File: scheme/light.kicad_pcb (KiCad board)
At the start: 2 copper layers, 25 parts, among them J1 Screw_Terminal_01x04 (buttons), J2 Conn_01x06_Male (programmer), J3 Screw_Terminal_01x06 (output), J4 Conn_01x02_Male (i2c), J5 Conn_01x02_Male (Jumper), J6 Conn_01x03_Male (Indicators), J7 Screw_Terminal_01x02 (power), Q1 IRF8308M, Q2 IRF8308M, Q3 IRF8308M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

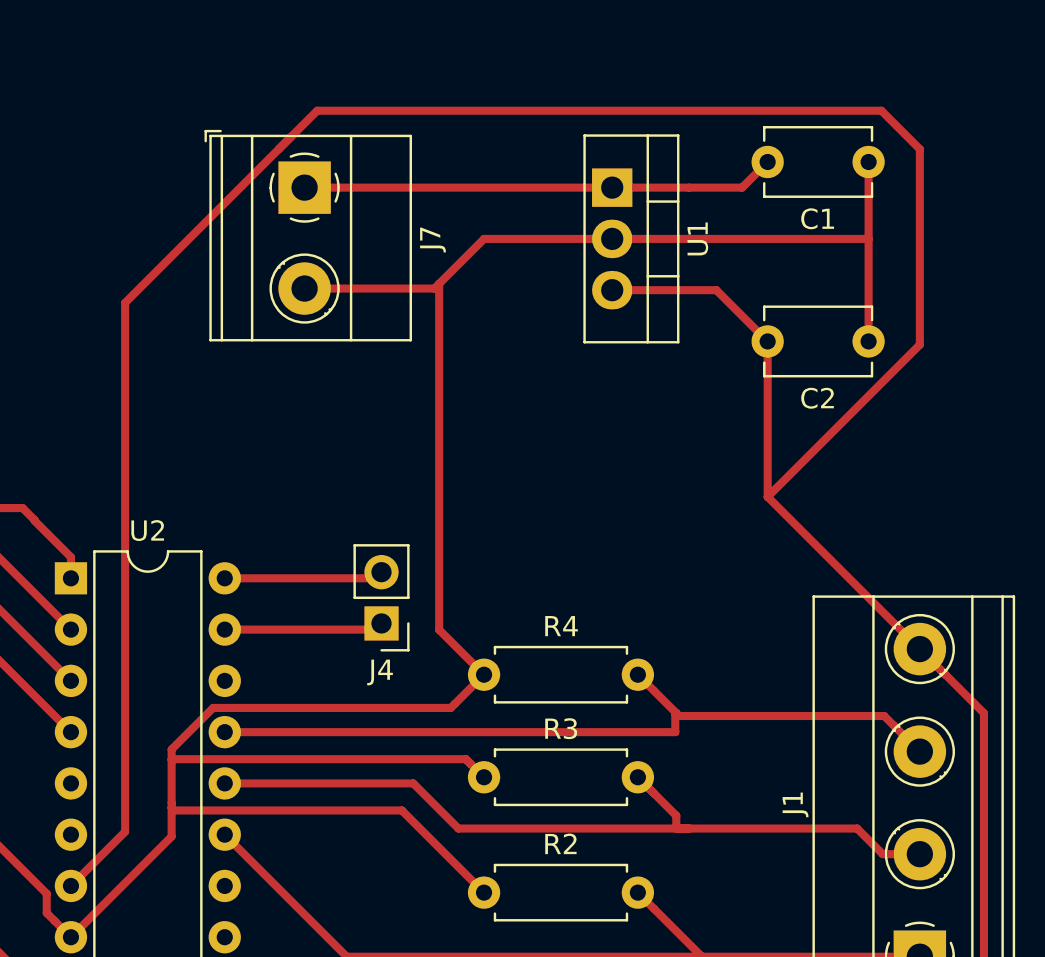
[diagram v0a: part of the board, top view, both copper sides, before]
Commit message: labels: fix power screw terminal orientation
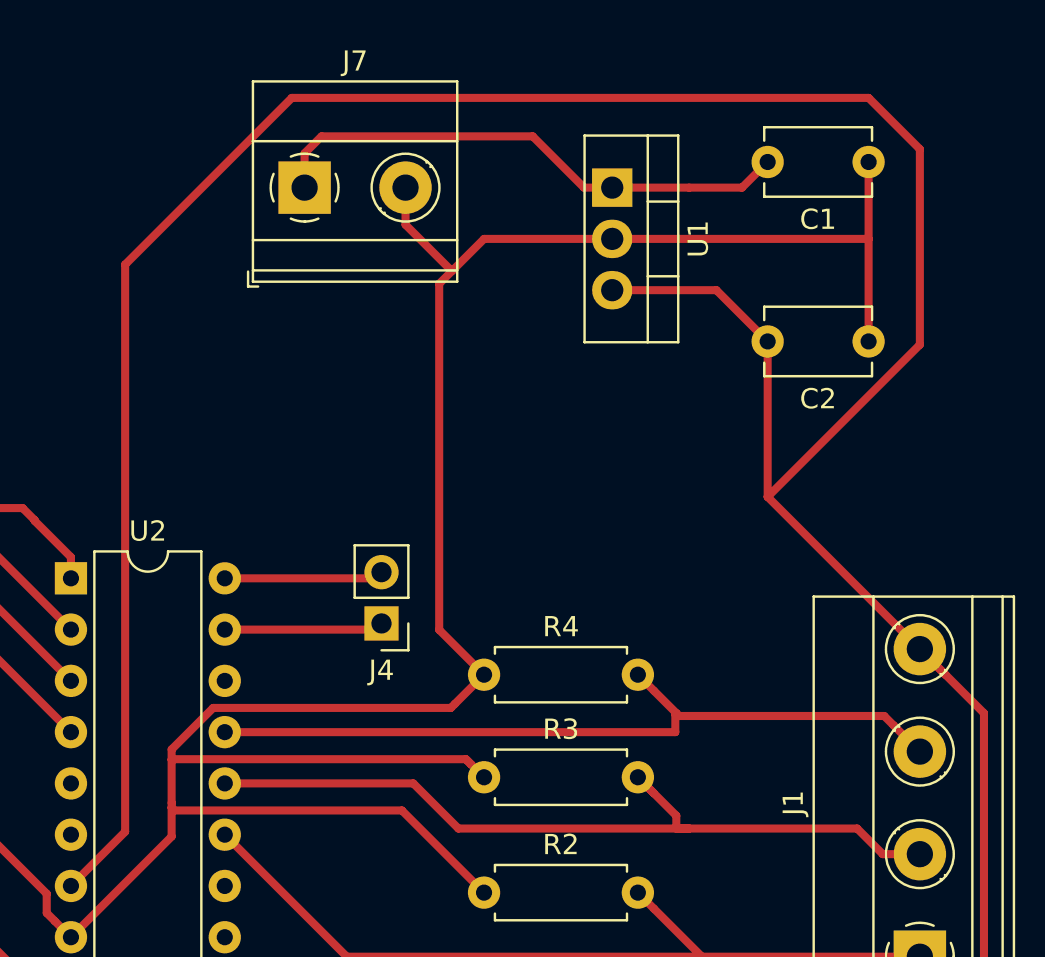
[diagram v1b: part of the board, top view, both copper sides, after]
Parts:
- turned J7 to 0 degrees
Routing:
- net Net-(C1-Pad2): track 23.5 -> 26.6 mm
- net GND: track 259.6 -> 257.9 mm
- net Net-(C2-Pad2): track 238.3 -> 239.1 mm
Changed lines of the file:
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@@
   (general
     (thickness 1.6)
-    (drawings 0)
-    (tracks 208)
+    (drawings 2)
+    (tracks 211)
     (zones 0)
     (modules 25)
@@
   )
   (module TerminalBlock_Phoenix:TerminalBlock_Phoenix_MKDS-1,5-2_1x02_P5.00mm_Horizontal (layer F.Cu)
-    (at 148.59 43.18 270)
+    (at 148.59 43.18)
     (descr "Terminal Block Phoenix MKDS-1,5-2, 2 pins, pitch 5mm, size 10x9.8mm^2, drill diamater 1.3mm, pad diameter 2.6mm, see http://www.farnell.com/datasheets/100425.pdf, script-generated using https://github.com/pointhi/kicad-footprint-generator/scripts/TerminalBlock_Phoenix")
     (tags "THT Terminal Block Phoenix MKDS-1,5-2 pitch 5mm size 10x9.8mm^2 drill 1.3mm pad 2.6mm")
-    (fp_text reference J7 (at 2.5 -6.26 90) (layer F.SilkS)
-      (effects (font (size 1 1) (thickness 0.15)))
-    )
-    (fp_text value "Screw_Terminal_01x02 (power)" (at 2.5 5.66 90) (layer F.Fab)
+    (fp_text reference J7 (at 2.5 -6.26) (layer F.SilkS)
+      (effects (font (size 1 1) (thickness 0.15)))
+    )
+    (fp_text value "Screw_Terminal_01x02 (power)" (at 2.5 5.66) (layer F.Fab)
       (effects (font (size 1 1) (thickness 0.15)))
     )
@@
     (fp_line (start 8 5.1) (end 8 -5.71) (layer F.CrtYd) (width 0.05))
     (fp_line (start 8 -5.71) (end -3 -5.71) (layer F.CrtYd) (width 0.05))
-    (fp_text user %R (at 2.5 3.2 90) (layer F.Fab)
-      (effects (font (size 1 1) (thickness 0.15)))
-    )
-    (pad 1 thru_hole rect (at 0 0 270) (size 2.6 2.6) (drill 1.3) (layers *.Cu *.Mask)
+    (fp_text user %R (at 2.5 3.2) (layer F.Fab)
+      (effects (font (size 1 1) (thickness 0.15)))
+    )
+    (pad 1 thru_hole rect (at 0 0) (size 2.6 2.6) (drill 1.3) (layers *.Cu *.Mask)
       (net 2 "Net-(C1-Pad2)"))
-    (pad 2 thru_hole circle (at 5 0 270) (size 2.6 2.6) (drill 1.3) (layers *.Cu *.Mask)
+    (pad 2 thru_hole circle (at 5 0) (size 2.6 2.6) (drill 1.3) (layers *.Cu *.Mask)
       (net 1 GND))
     (model ${KISYS3DMOD}/TerminalBlock_Phoenix.3dshapes/TerminalBlock_Phoenix_MKDS-1,5-2_1x02_P5.00mm_Horizontal.wrl
@@
     )
   )
+  (dimension 85.725 (width 0.15) (layer F.SilkS)
+    (gr_text "85.725 mm" (at 192.435 80.9625 270) (layer F.SilkS)
+      (effects (font (size 1 1) (thickness 0.15)))
+    )
+    (feature1 (pts (xy 177.8 123.825) (xy 191.721421 123.825)))
+    (feature2 (pts (xy 177.8 38.1) (xy 191.721421 38.1)))
+    (crossbar (pts (xy 191.135 38.1) (xy 191.135 123.825)))
+    (arrow1a (pts (xy 191.135 123.825) (xy 190.548579 122.698496)))
+    (arrow1b (pts (xy 191.135 123.825) (xy 191.721421 122.698496)))
+    (arrow2a (pts (xy 191.135 38.1) (xy 190.548579 39.226504)))
+    (arrow2b (pts (xy 191.135 38.1) (xy 191.721421 39.226504)))
+  )
+  (dimension 99.241 (width 0.15) (layer F.SilkS)
+    (gr_text "99.241 mm" (at 134.5295 30.45) (layer F.SilkS)
+      (effects (font (size 1 1) (thickness 0.15)))
+    )
+    (feature1 (pts (xy 184.15 72.33) (xy 184.15 31.163579)))
+    (feature2 (pts (xy 84.909 72.33) (xy 84.909 31.163579)))
+    (crossbar (pts (xy 84.909 31.75) (xy 184.15 31.75)))
+    (arrow1a (pts (xy 184.15 31.75) (xy 183.023496 32.336421)))
+    (arrow1b (pts (xy 184.15 31.75) (xy 183.023496 31.163579)))
+    (arrow2a (pts (xy 84.909 31.75) (xy 86.035504 32.336421)))
+    (arrow2b (pts (xy 84.909 31.75) (xy 86.035504 31.163579)))
+  )
   (segment (start 176.53 45.72) (end 163.83 45.72) (width 0.4) (layer F.Cu) (net 1))
   (segment (start 176.53 45.72) (end 176.53 50.8) (width 0.4) (layer F.Cu) (net 1))
   (segment (start 176.53 41.91) (end 176.53 45.72) (width 0.4) (layer F.Cu) (net 1))
-  (segment (start 148.59 48.18) (end 155.02 48.18) (width 0.4) (layer F.Cu) (net 1))
   (segment (start 157.48 45.72) (end 163.83 45.72) (width 0.4) (layer F.Cu) (net 1))
   (segment (start 155.2575 65.0875) (end 157.48 67.31) (width 0.4) (layer F.Cu) (net 1))
   (segment (start 155.2575 47.9425) (end 155.2575 65.0875) (width 0.4) (layer F.Cu) (net 1))
-  (segment (start 155.2575 47.9425) (end 157.48 45.72) (width 0.4) (layer F.Cu) (net 1))
-  (segment (start 155.02 48.18) (end 155.2575 47.9425) (width 0.4) (layer F.Cu) (net 1))
   (segment (start 137.015001 80.315001) (end 142.002501 75.327501) (width 0.4) (layer F.Cu) (net 1))
   (segment (start 109.22 97.79) (end 110.49 96.52) (width 0.4) (layer F.Cu) (net 1))
@@
   (segment (start 119.775002 69.85) (end 119.895001 69.969999) (width 0.4) (layer F.Cu) (net 1))
   (segment (start 119.895001 69.969999) (end 123.070001 73.144999) (width 0.4) (layer F.Cu) (net 1))
-  (segment (start 148.59 43.18) (end 163.83 43.18) (width 0.4) (layer F.Cu) (net 2))
+  (segment (start 155.879023 47.3075) (end 155.8925 47.3075) (width 0.4) (layer F.Cu) (net 1))
+  (segment (start 153.59 45.018477) (end 155.879023 47.3075) (width 0.4) (layer F.Cu) (net 1))
+  (segment (start 153.59 43.18) (end 153.59 45.018477) (width 0.4) (layer F.Cu) (net 1))
+  (segment (start 155.2575 47.9425) (end 155.8925 47.3075) (width 0.4) (layer F.Cu) (net 1))
+  (segment (start 155.8925 47.3075) (end 157.48 45.72) (width 0.4) (layer F.Cu) (net 1))
   (segment (start 163.83 43.18) (end 167.64 43.18) (width 0.4) (layer F.Cu) (net 2))
   (segment (start 170.26 43.18) (end 171.53 41.91) (width 0.4) (layer F.Cu) (net 2))
   (segment (start 167.64 43.18) (end 170.26 43.18) (width 0.4) (layer F.Cu) (net 2))
+  (segment (start 148.59 41.48) (end 149.43 40.64) (width 0.4) (layer F.Cu) (net 2))
+  (segment (start 148.59 43.18) (end 148.59 41.48) (width 0.4) (layer F.Cu) (net 2))
+  (segment (start 162.43 43.18) (end 163.83 43.18) (width 0.4) (layer F.Cu) (net 2))
+  (segment (start 159.89 40.64) (end 162.43 43.18) (width 0.4) (layer F.Cu) (net 2))
+  (segment (start 149.43 40.64) (end 159.89 40.64) (width 0.4) (layer F.Cu) (net 2))
   (segment (start 168.99 48.26) (end 171.53 50.8) (width 0.4) (layer F.Cu) (net 3))
   (segment (start 163.83 48.26) (end 168.99 48.26) (width 0.4) (layer F.Cu) (net 3))
   (segment (start 171.53 58.5) (end 179.07 66.04) (width 0.4) (layer F.Cu) (net 3))
   (segment (start 171.53 50.8) (end 171.53 58.5) (width 0.4) (layer F.Cu) (net 3))
-  (segment (start 137.015001 77.775001) (end 139.7 75.090002) (width 0.4) (layer F.Cu) (net 3))
-  (segment (start 139.7 75.090002) (end 139.7 48.884998) (width 0.4) (layer F.Cu) (net 3))
   (segment (start 180.369999 67.339999) (end 179.07 66.04) (width 0.4) (layer F.Cu) (net 3))
   (segment (start 152.4 102.235) (end 153.199999 103.034999) (width 0.4) (layer F.Cu) (net 3))
@@
   (segment (start 182.245 69.215) (end 179.07 66.04) (width 0.4) (layer F.Cu) (net 3))
   (segment (start 182.245 88.265) (end 182.245 69.215) (width 0.4) (layer F.Cu) (net 3))
-  (segment (start 147.944998 40.64) (end 147.314999 41.269999) (width 0.4) (layer F.Cu) (net 3))
-  (segment (start 139.7 48.884998) (end 147.314999 41.269999) (width 0.4) (layer F.Cu) (net 3))
   (segment (start 148.618001 121.202001) (end 160.184999 109.635003) (width 0.4) (layer F.Cu) (net 3))
   (segment (start 129.559999 120.669999) (end 130.092001 121.202001) (width 0.4) (layer F.Cu) (net 3))
@@
   (segment (start 160.184999 109.635003) (end 160.184999 103.034999) (width 0.4) (layer F.Cu) (net 3))
   (segment (start 129.559999 116.999999) (end 129.559999 120.669999) (width 0.4) (layer F.Cu) (net 3))
-  (segment (start 147.799999 40.784999) (end 147.314999 41.269999) (width 0.4) (layer F.Cu) (net 3))
-  (segment (start 179.07 50.96) (end 179.07 41.275) (width 0.4) (layer F.Cu) (net 3))
-  (segment (start 171.53 58.5) (end 179.07 50.96) (width 0.4) (layer F.Cu) (net 3))
-  (segment (start 179.07 41.275) (end 177.165 39.37) (width 0.4) (layer F.Cu) (net 3))
-  (segment (start 177.165 39.37) (end 149.214998 39.37) (width 0.4) (layer F.Cu) (net 3))
-  (segment (start 149.214998 39.37) (end 147.799999 40.784999) (width 0.4) (layer F.Cu) (net 3))
+  (segment (start 179.07 50.96) (end 171.53 58.5) (width 0.4) (layer F.Cu) (net 3))
+  (segment (start 179.07 41.275) (end 179.07 50.96) (width 0.4) (layer F.Cu) (net 3))
+  (segment (start 139.7 75.090002) (end 139.7 46.99) (width 0.4) (layer F.Cu) (net 3))
+  (segment (start 176.53 38.735) (end 179.07 41.275) (width 0.4) (layer F.Cu) (net 3))
+  (segment (start 137.015001 77.775001) (end 139.7 75.090002) (width 0.4) (layer F.Cu) (net 3))
+  (segment (start 147.955 38.735) (end 176.53 38.735) (width 0.4) (layer F.Cu) (net 3))
+  (segment (start 139.7 46.99) (end 147.955 38.735) (width 0.4) (layer F.Cu) (net 3))
   (segment (start 144.635001 75.235001) (end 150.68 81.28) (width 0.4) (layer F.Cu) (net 4))
   (segment (start 165.899999 78.904999) (end 168.275 81.28) (width 0.4) (layer F.Cu) (net 4))

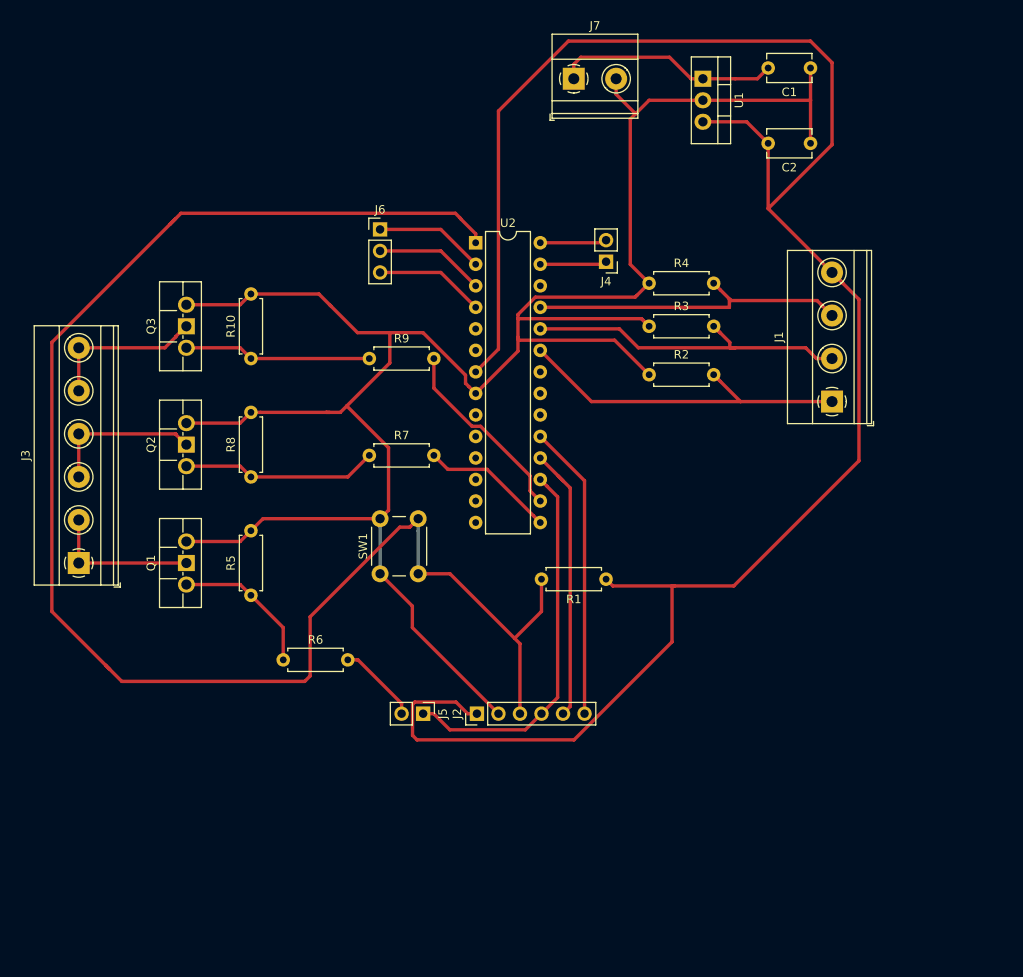
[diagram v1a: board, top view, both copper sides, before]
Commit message: scheme: change routes widths
And avoid between pins routes
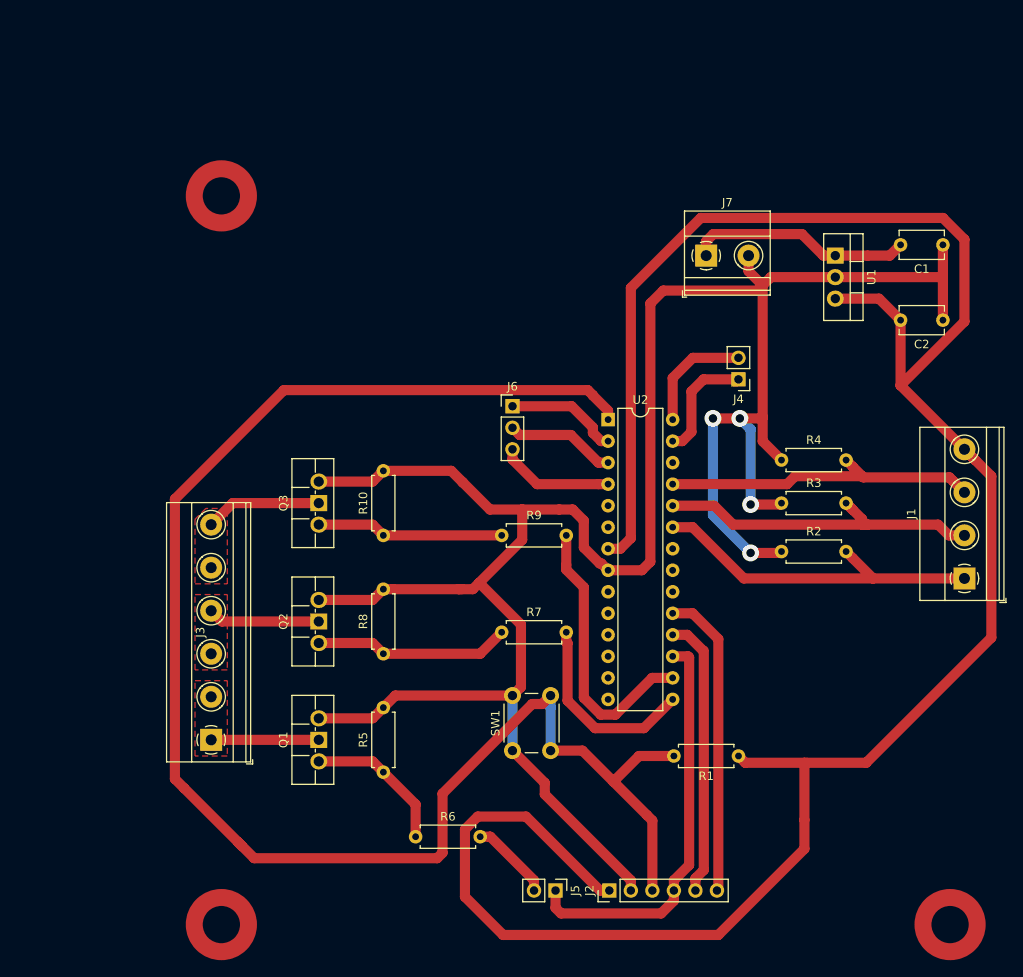
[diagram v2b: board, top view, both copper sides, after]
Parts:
- moved R7 26.1 mm to (140.1, 108.5)
- moved C1 26.1 mm to (192.2, 62.8)
- moved C2 26.1 mm to (192.2, 71.7)
- moved J1 26.1 mm to (194.7, 102.2)
- moved J3 26.1 mm to (105.8, 121.2)
- moved R1 26.1 mm to (168.0, 123.1)
- moved R3 26.1 mm to (173.1, 93.3)
- moved R4 26.1 mm to (173.1, 88.2)
- moved R5 26.1 mm to (126.1, 125.0)
- moved R8 26.1 mm to (126.1, 111.0)
- moved R6 26.1 mm to (129.9, 132.6)
- moved R9 26.1 mm to (140.1, 97.1)
- moved J7 26.1 mm to (164.2, 64.0)
- moved SW1 26.1 mm to (141.4, 122.5)
- moved U1 26.1 mm to (179.5, 64.0)
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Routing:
- net Net-(C2-Pad2): track 239.1 -> 271.3 mm
- net GND: track 257.9 -> 289.1 mm, vias 0 -> 4
- net Net-(R9-Pad2): track 23.4 -> 33.1 mm
- net Net-(R7-Pad2): track 15.8 -> 23.3 mm
- net Net-(J4-Pad1): track 7.89 -> 14.0 mm
- net Net-(J4-Pad2): track 7.89 -> 13.7 mm
- net Net-(J3-Pad1): track 17.8 -> 12.7 mm
- net Net-(J3-Pad3): track 18.3 -> 13.3 mm
- net Net-(J3-Pad5): track 18.9 -> 14.6 mm
- net Net-(J2-Pad4): track 44.8 -> 48.4 mm
- net Net-(J2-Pad3): track 188.9 -> 191.1 mm
- net Net-(J2-Pad6): track 34.9 -> 36.4 mm
- net Net-(J6-Pad3): track 13.0 -> 13.7 mm
- added copper zone on F.Cu, net Net-(J3-Pad1)
- added copper zone on F.Cu, net Net-(J3-Pad3)
- added copper zone on F.Cu, net Net-(J3-Pad5)
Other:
- net class 12v added: clearance 0.2, trace_width 0.8, via_dia 1, via_drill 0.8
- net class Default: clearance 0.2 -> 0.4
- rule trace_clearance: 0.2 -> 0.4
